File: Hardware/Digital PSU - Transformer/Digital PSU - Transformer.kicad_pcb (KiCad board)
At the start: 2 copper layers, 82.2 x 85 mm, 10 parts, among them J10 18V AC, J11 18V AC, J4 15V AC, J5 230V AC

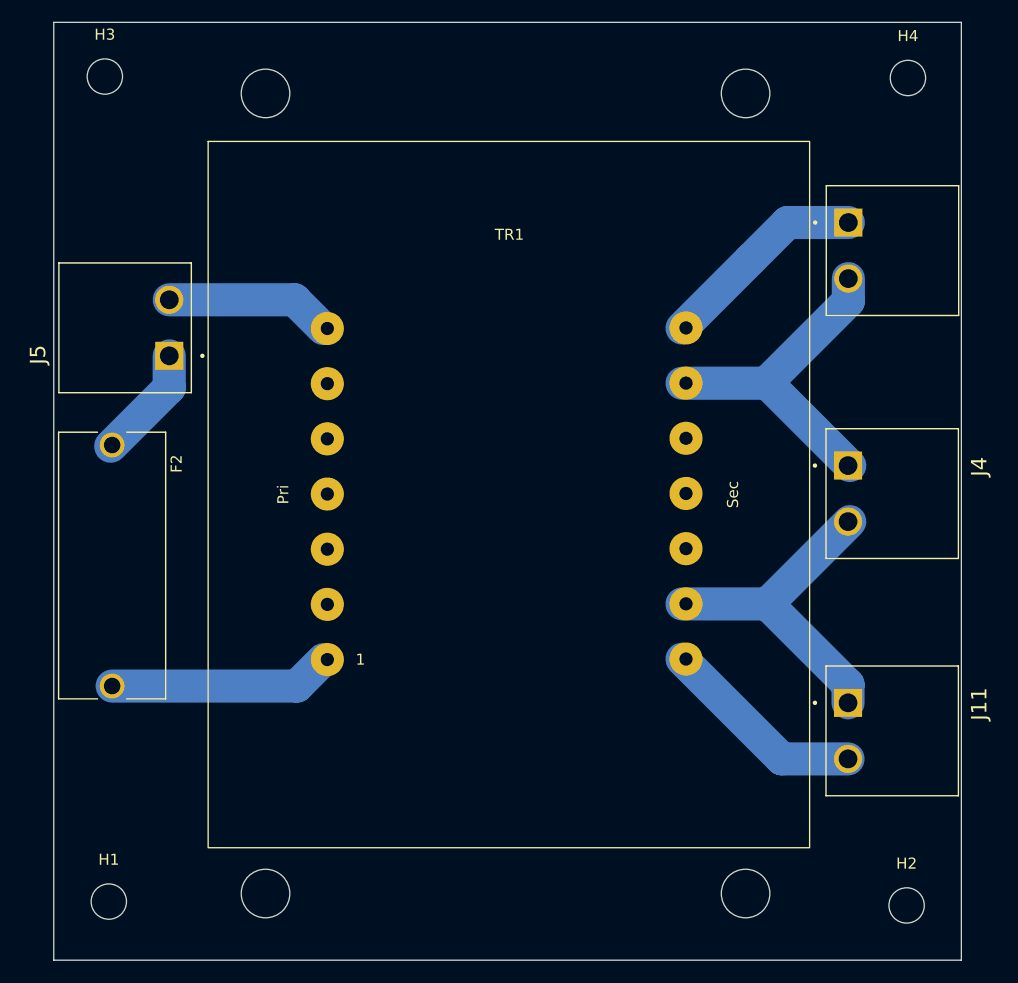
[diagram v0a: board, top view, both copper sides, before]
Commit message: Ready for review (updated Digital PSU - Transformer and Controller)
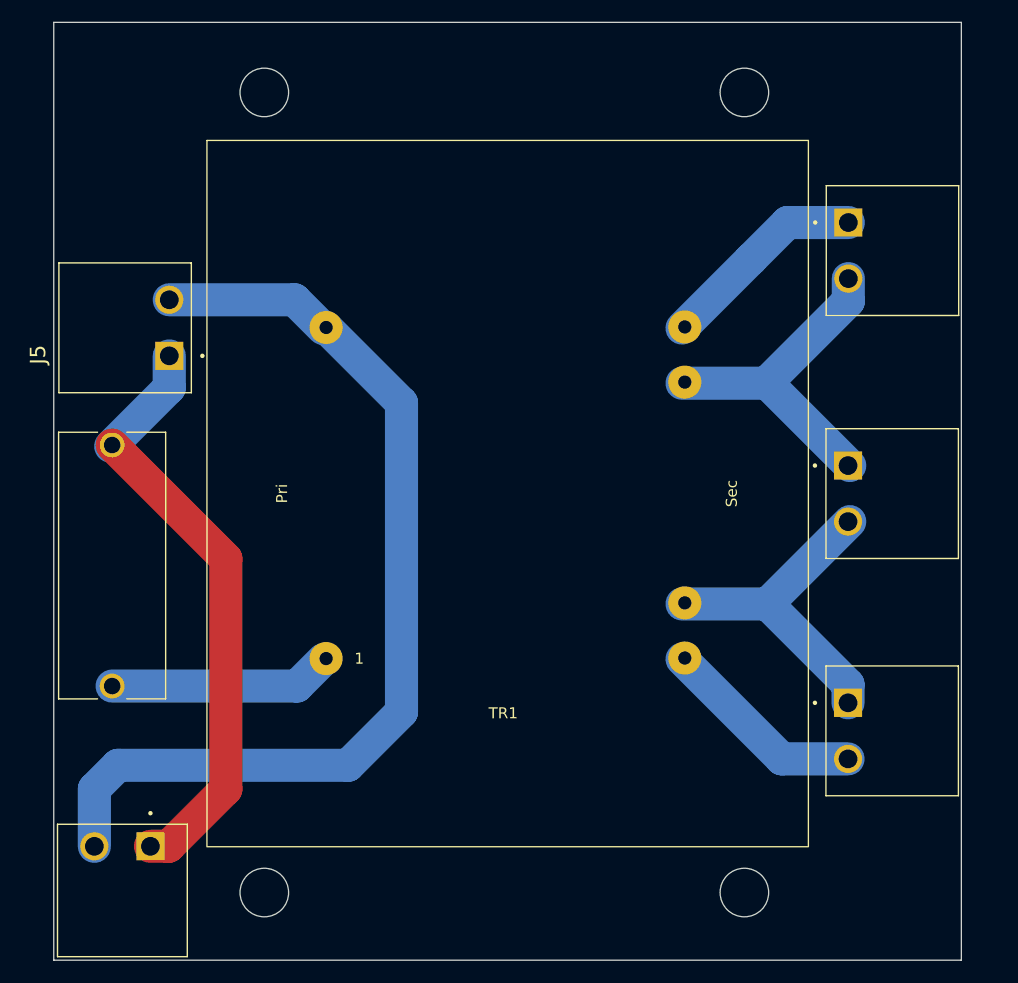
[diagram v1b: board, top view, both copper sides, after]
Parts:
- removed H1, H2, H3, H4: MountingHole, MountingHole:MountingHole_3.2mm_M3_DIN965
- added J1: 230V AC, THE_PREAMP_CONN_POWER_5_08:TBP01R1-508-02BK, F.Cu at (24.6, 100.7)
- TR1: footprint Transformer_Hahn_BV_EL_603_1027:Transformer_Hahn_BV_EL_603_1027 -> Transformer_Hahn_BV_EL_603_1027:Transformer_Hahn_BV_EL_603_COMBINED
- moved TR1 15.7 mm to (56.6, 89.1)
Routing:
- net Net-(J1-Pin_2): track 15.0 -> 88.6 mm
- net Net-(J1-Pin_1): track 10.4 -> 54.8 mm
